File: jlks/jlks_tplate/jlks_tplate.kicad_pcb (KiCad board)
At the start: 2 copper layers, 114.3 x 99.4 mm, 21 parts, among them SW0 SW_Push, SW1 SW_Push, SW10 SW_Push, SW11 SW_Push, SW12 SW_Push, SW13 SW_Push, SW14 SW_Push, SW15 SW_Push, SW16 SW_Push, SW2 SW_Push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

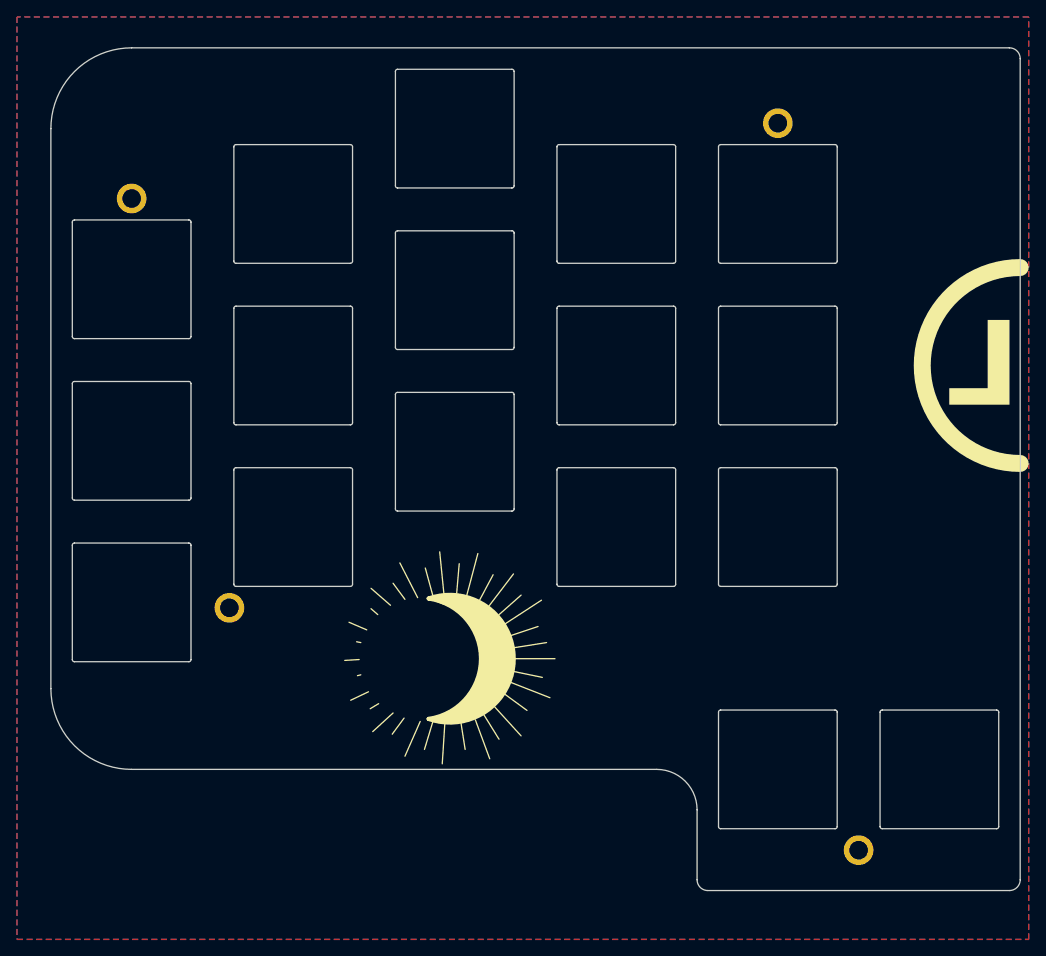
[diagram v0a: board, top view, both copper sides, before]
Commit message: Moved some of the mounting holes around.
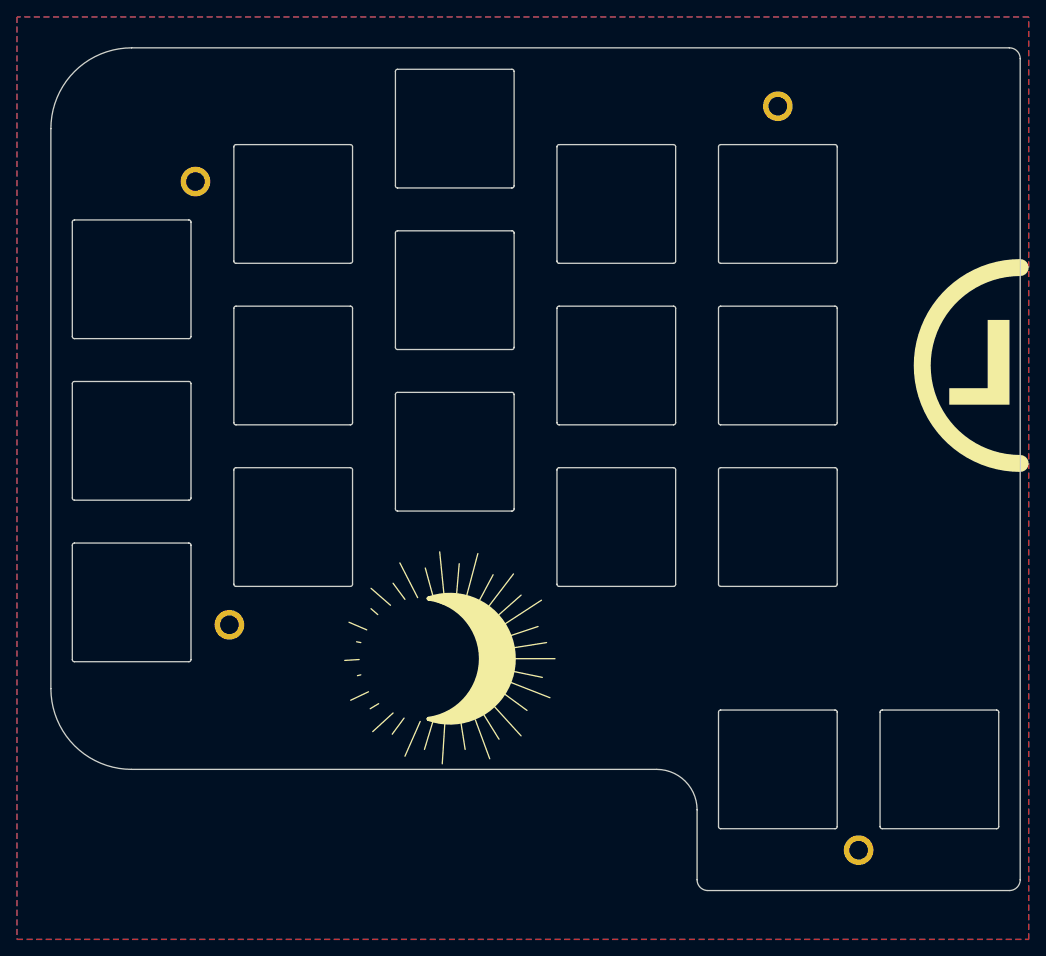
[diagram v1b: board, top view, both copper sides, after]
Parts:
- moved H1 7.79 mm to (74.2, 64.0)
- moved H0 2.00 mm to (142.9, 55.1)
- moved H2 2.00 mm to (78.2, 116.3)
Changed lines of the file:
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@@
   (net 1 "GND")
   (footprint "MountingHole:MountingHole_2.2mm_M2_ISO7380_Pad" (layer "F.Cu")
-    (at 78.2 114.3)
+    (at 78.2 116.3)
     (descr "Mounting Hole 2.2mm, M2, ISO7380")
     (tags "mounting hole 2.2mm m2 iso7380")
@@
   )
   (footprint "MountingHole:MountingHole_2.2mm_M2_ISO7380_Pad" (layer "F.Cu")
-    (at 142.875 57.15)
+    (at 142.875 55.15)
     (descr "Mounting Hole 2.2mm, M2, ISO7380")
     (tags "mounting hole 2.2mm m2 iso7380")
@@
   )
   (footprint "MountingHole:MountingHole_2.2mm_M2_ISO7380_Pad" (layer "F.Cu")
-    (at 66.675 66.033161)
+    (at 74.2 64.033161)
     (descr "Mounting Hole 2.2mm, M2, ISO7380")
     (tags "mounting hole 2.2mm m2 iso7380")

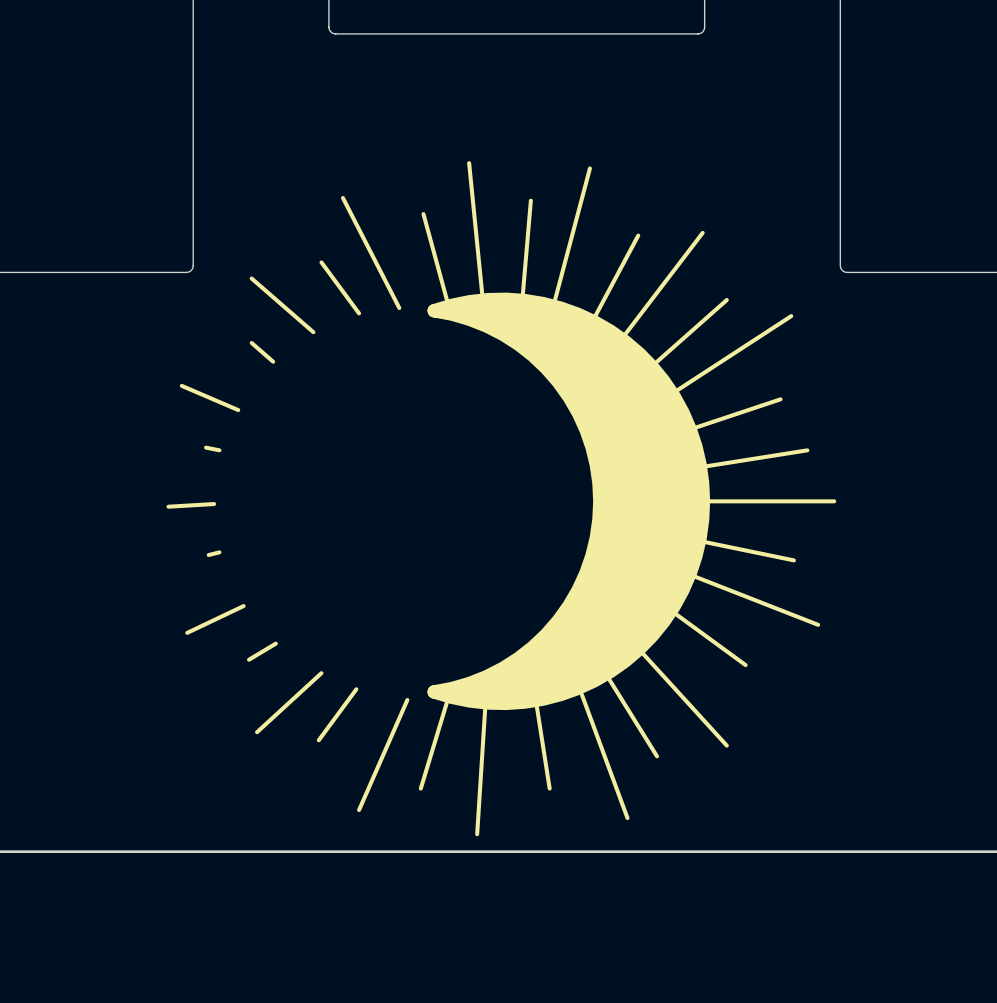
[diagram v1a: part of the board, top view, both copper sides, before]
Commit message: Small modifications to the top and bottom plates.
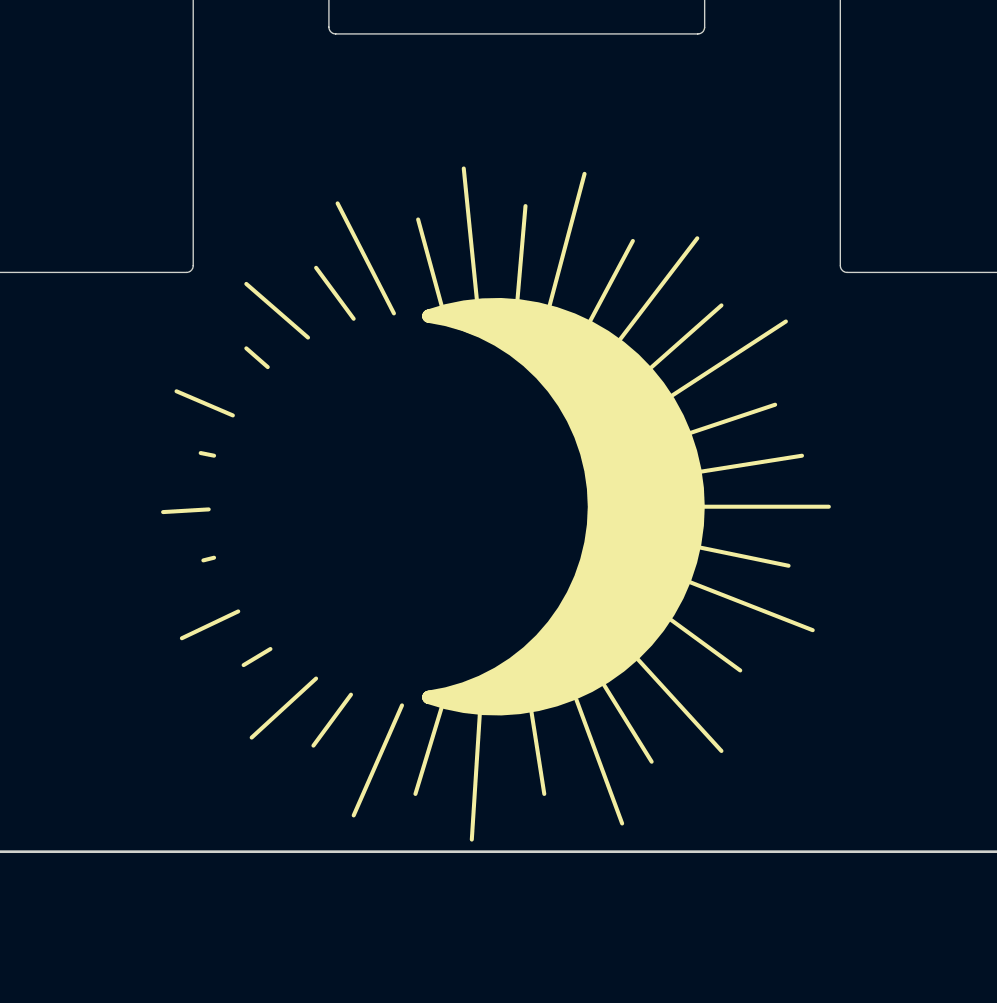
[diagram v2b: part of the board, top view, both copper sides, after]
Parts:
- added REF**: eclipse_logo, footprints:eclipse_logo, F.Cu at (104.0, 120.5)
- added REF**: moon_logo, footprints:moon_logo, B.Cu at (104.0, 120.5)
